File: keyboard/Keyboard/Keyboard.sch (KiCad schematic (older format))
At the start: 44 parts, among them J1 Conn_01x04, SW1 1, SW2 2, SW3 3, SW4 4, SW5 5, SW7 6, U1 TCA8418

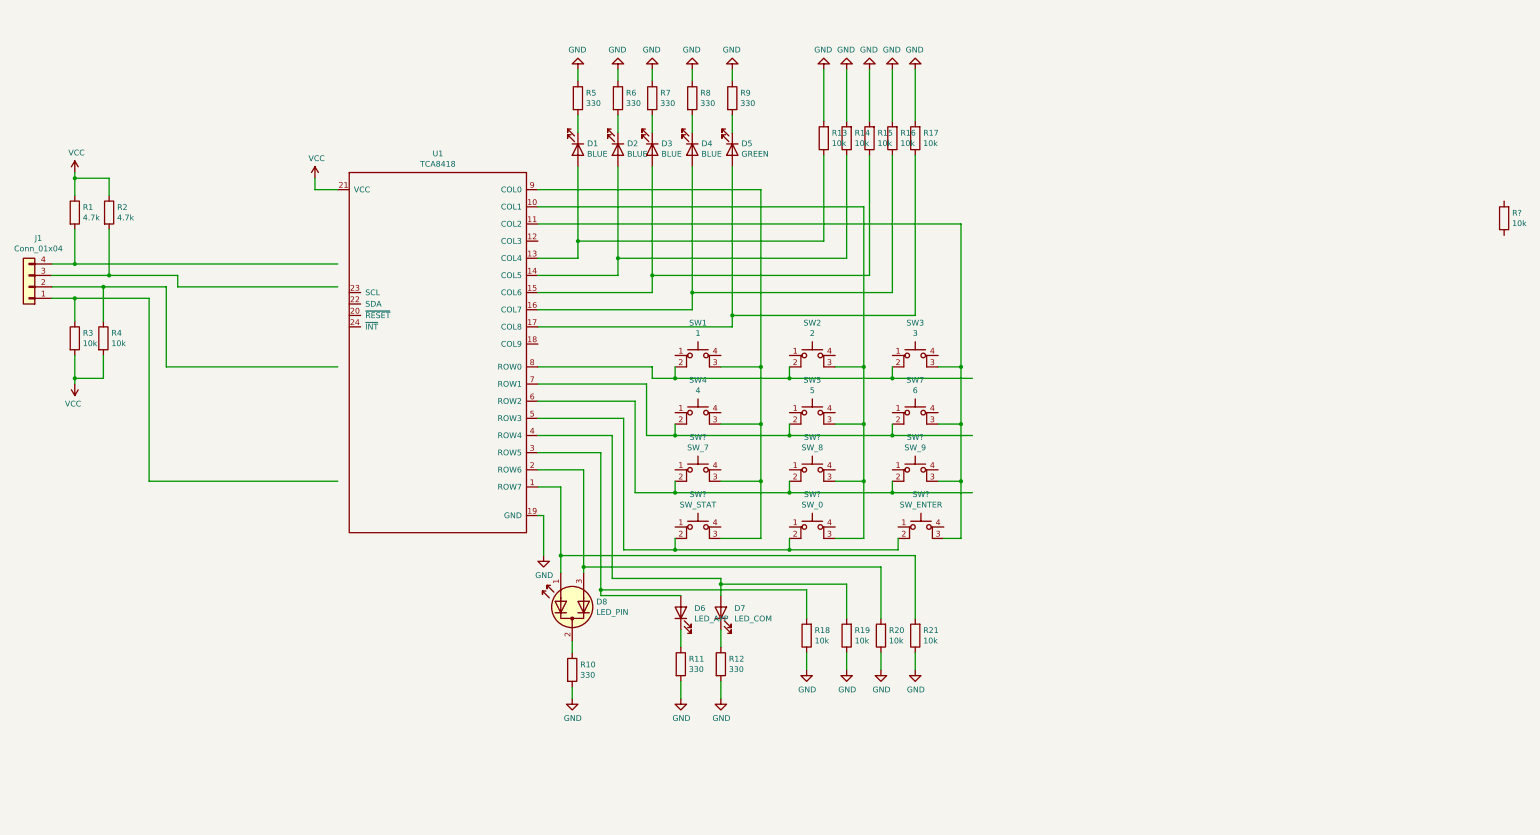
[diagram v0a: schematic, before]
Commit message: fixed pin number, added vcc, gnd header
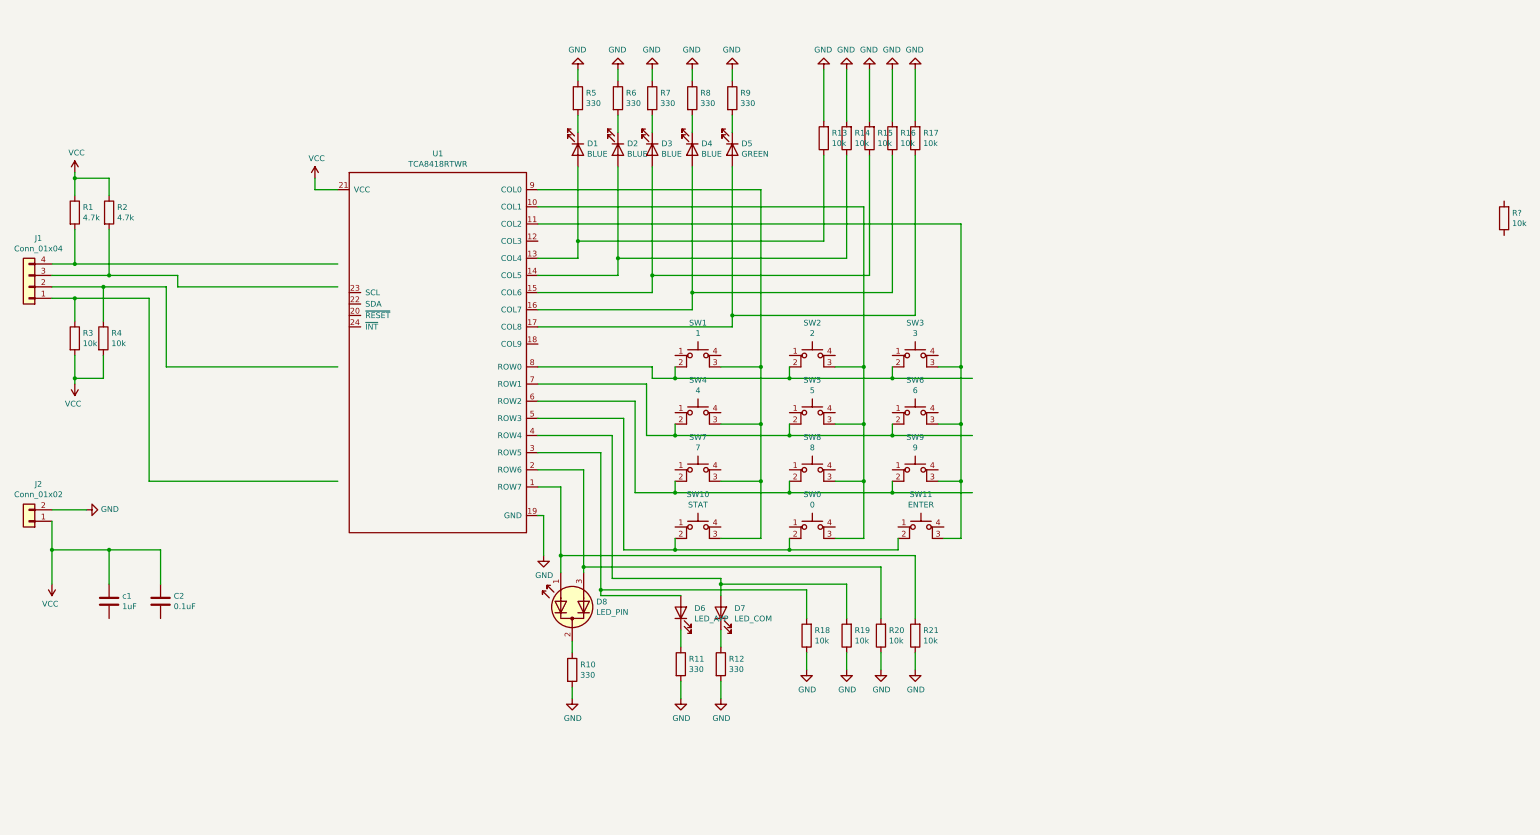
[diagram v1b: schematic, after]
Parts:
- added C2: 0.1uF, symbol Device:C
- added J2: Conn_01x02, symbol Connector_Generic:Conn_01x02
- added c1: 1uF, symbol Device:C
- SW0: renamed from SW?; value SW_0 -> 0
- SW10: renamed from SW?; value SW_STAT -> STAT
- SW11: renamed from SW?; value SW_ENTER -> ENTER
- SW7: renamed from SW?; value SW_7 -> 7
- SW8: renamed from SW?; value SW_8 -> 8
- SW9: renamed from SW?; value SW_9 -> 9
- U1: value TCA8418 -> TCA8418RTWR
- renumbered SW7 to SW6
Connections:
- wire segments 165 -> 172
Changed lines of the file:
@@
 Sheet 1 1
 Title "MixMesh keyboard"
-Date "2020-12-14"
-Rev "1.0"
+Date "2020-12-17"
+Rev "1.1"
 Comp "MixMesh"
 Comment1 ""
@@
 P 4250 3450
 F 0 "U1" H 4275 5215 50  0000 C CNN
-F 1 "TCA8418" H 4275 5124 50  0000 C CNN
+F 1 "TCA8418RTWR" H 4275 5124 50  0000 C CNN
 F 2 "" H 1300 2550 50  0001 C CNN
 F 3 "" H 1300 2550 50  0001 C CNN
@@
 $EndComp
 $Comp
-L Switch:SW_MEC_5E SW7
+L Switch:SW_MEC_5E SW6
 U 1 1 5FC76FF5
 P 8450 4050
-F 0 "SW7" H 8450 4435 50  0000 C CNN
+F 0 "SW6" H 8450 4435 50  0000 C CNN
 F 1 "6" H 8450 4344 50  0000 C CNN
 F 2 "" H 8450 4350 50  0001 C CNN
@@
 $EndComp
 $Comp
-L Switch:SW_MEC_5E SW?
+L Switch:SW_MEC_5E SW7
 U 1 1 5FC778BD
 P 6550 4550
-F 0 "SW?" H 6550 4935 50  0000 C CNN
-F 1 "SW_7" H 6550 4844 50  0000 C CNN
+F 0 "SW7" H 6550 4935 50  0000 C CNN
+F 1 "7" H 6550 4844 50  0000 C CNN
 F 2 "" H 6550 4850 50  0001 C CNN
 F 3 "http://www.apem.com/int/index.php?controller=attachment&id_attachment=1371" H 6550 4850 50  0001 C CNN
@@
 $EndComp
 $Comp
-L Switch:SW_MEC_5E SW?
+L Switch:SW_MEC_5E SW8
 U 1 1 5FC7801D
 P 7550 4550
-F 0 "SW?" H 7550 4935 50  0000 C CNN
-F 1 "SW_8" H 7550 4844 50  0000 C CNN
+F 0 "SW8" H 7550 4935 50  0000 C CNN
+F 1 "8" H 7550 4844 50  0000 C CNN
 F 2 "" H 7550 4850 50  0001 C CNN
 F 3 "http://www.apem.com/int/index.php?controller=attachment&id_attachment=1371" H 7550 4850 50  0001 C CNN
@@
 $EndComp
 $Comp
-L Switch:SW_MEC_5E SW?
+L Switch:SW_MEC_5E SW9
 U 1 1 5FC78EF4
 P 8450 4550
-F 0 "SW?" H 8450 4935 50  0000 C CNN
-F 1 "SW_9" H 8450 4844 50  0000 C CNN
+F 0 "SW9" H 8450 4935 50  0000 C CNN
+F 1 "9" H 8450 4844 50  0000 C CNN
 F 2 "" H 8450 4850 50  0001 C CNN
 F 3 "http://www.apem.com/int/index.php?controller=attachment&id_attachment=1371" H 8450 4850 50  0001 C CNN
@@
 $EndComp
 $Comp
-L Switch:SW_MEC_5E SW?
+L Switch:SW_MEC_5E SW10
 U 1 1 5FC79FBB
 P 6550 5050
-F 0 "SW?" H 6550 5435 50  0000 C CNN
-F 1 "SW_STAT" H 6550 5344 50  0000 C CNN
+F 0 "SW10" H 6550 5435 50  0000 C CNN
+F 1 "STAT" H 6550 5344 50  0000 C CNN
 F 2 "" H 6550 5350 50  0001 C CNN
 F 3 "http://www.apem.com/int/index.php?controller=attachment&id_attachment=1371" H 6550 5350 50  0001 C CNN
@@
 $EndComp
 $Comp
-L Switch:SW_MEC_5E SW?
+L Switch:SW_MEC_5E SW0
 U 1 1 5FC7A322
 P 7550 5050
-F 0 "SW?" H 7550 5435 50  0000 C CNN
-F 1 "SW_0" H 7550 5344 50  0000 C CNN
+F 0 "SW0" H 7550 5435 50  0000 C CNN
+F 1 "0" H 7550 5344 50  0000 C CNN
 F 2 "" H 7550 5350 50  0001 C CNN
 F 3 "http://www.apem.com/int/index.php?controller=attachment&id_attachment=1371" H 7550 5350 50  0001 C CNN
@@
 $EndComp
 $Comp
-L Switch:SW_MEC_5E SW?
+L Switch:SW_MEC_5E SW11
 U 1 1 5FC7A6C1
 P 8500 5050
-F 0 "SW?" H 8500 5435 50  0000 C CNN
-F 1 "SW_ENTER" H 8500 5344 50  0000 C CNN
+F 0 "SW11" H 8500 5435 50  0000 C CNN
+F 1 "ENTER" H 8500 5344 50  0000 C CNN
 F 2 "" H 8500 5350 50  0001 C CNN
 F 3 "http://www.apem.com/int/index.php?controller=attachment&id_attachment=1371" H 8500 5350 50  0001 C CNN
@@
 	5150 2150 8000 2150
 Wire Wire Line
-	8000 2150 8000 3550
-Wire Wire Line
 	5150 2300 8850 2300
-Wire Wire Line
-	8850 2300 8850 3550
 Wire Wire Line
 	8650 3550 8850 3550
@@
 Wire Wire Line
 	7750 3550 8000 3550
-Connection ~ 8000 3550
 Wire Wire Line
 	8000 3550 8000 4050
@@
 	5850 2750 5150 2750
 Wire Wire Line
-	6150 1800 6150 2750
-Wire Wire Line
 	6150 2900 5150 2900
 Wire Wire Line
@@
 Wire Wire Line
 	8850 5050 8700 5050
-Connection ~ 8850 3550
 Wire Wire Line
 	8650 4050 8850 4050
@@
 	5500 2450 5500 2600
 Wire Wire Line
-	5850 1800 5850 2600
-Connection ~ 5850 2600
-Wire Wire Line
-	5850 2600 5850 2750
-Wire Wire Line
-	8050 1700 8050 2750
-Wire Wire Line
-	8050 2750 6150 2750
-Connection ~ 6150 2750
-Wire Wire Line
-	6150 2750 6150 2900
-Wire Wire Line
-	8450 1700 8450 3100
-Wire Wire Line
 	8450 3100 6850 3100
 Connection ~ 6850 3100
@@
 	6850 3100 6850 3200
 Wire Wire Line
-	8250 1700 8250 2900
-Wire Wire Line
 	8250 2900 6500 2900
 Connection ~ 6500 2900
 Wire Wire Line
 	6500 2900 6500 3050
-Wire Wire Line
-	7850 1700 7850 2600
-Wire Wire Line
-	5850 2600 7850 2600
 Wire Wire Line
 	7650 1700 7650 2450
@@
 Wire Wire Line
 	5350 5200 5350 5350
+$Comp
+L Device:C c1
+U 1 1 5FDC4FA0
+P 1400 5600
+F 0 "c1" H 1515 5646 50  0000 L CNN
+F 1 "1uF" H 1515 5555 50  0000 L CNN
+F 2 "" H 1438 5450 50  0001 C CNN
+F 3 "~" H 1400 5600 50  0001 C CNN
+	1    1400 5600
+	1    0    0    -1
+$EndComp
+$Comp
+L Device:C C2
+U 1 1 5FDC5C48
+P 1850 5600
+F 0 "C2" H 1965 5646 50  0000 L CNN
+F 1 "0.1uF" H 1965 5555 50  0000 L CNN
+F 2 "" H 1888 5450 50  0001 C CNN
+F 3 "~" H 1850 5600 50  0001 C CNN
+	1    1850 5600
+	1    0    0    -1
+$EndComp
+$Comp
+L Connector_Generic:Conn_01x02 J2
+U 1 1 5FDDA441
+P 700 4900
+F 0 "J2" H 618 4575 50  0000 C CNN
+F 1 "Conn_01x02" H 618 4666 50  0000 C CNN
+F 2 "" H 700 4900 50  0001 C CNN
+F 3 "~" H 700 4900 50  0001 C CNN
+	1    700  4900
+	-1   0    0    1
+$EndComp
+$Comp
+L power:VCC #PWR?
+U 1 1 5FDDCD5B
+P 900 5450
+F 0 "#PWR?" H 900 5300 50  0001 C CNN
+F 1 "VCC" H 915 5623 50  0000 C CNN
+F 2 "" H 900 5450 50  0001 C CNN
+F 3 "" H 900 5450 50  0001 C CNN
+	1    900  5450
+	-1   0    0    1
+$EndComp
+Connection ~ 6150 2750
+Connection ~ 5850 2600
+Wire Wire Line
+	5850 2600 5850 2750
+Wire Wire Line
+	5850 1800 5850 2600
+Connection ~ 8850 3550
+Wire Wire Line
+	6150 2750 6150 2900
+Wire Wire Line
+	6150 1800 6150 2750
+Connection ~ 8000 3550
+Wire Wire Line
+	5850 2600 7850 2600
+Wire Wire Line
+	7850 1700 7850 2600
+Wire Wire Line
+	8250 1700 8250 2900
+Wire Wire Line
+	8450 1700 8450 3100
+Wire Wire Line
+	8050 2750 6150 2750
+Wire Wire Line
+	8050 1700 8050 2750
+Wire Wire Line
+	8850 2300 8850 3550
+Wire Wire Line
+	8000 2150 8000 3550
+$Comp
+L power:GND #PWR?
+U 1 1 5FE49D2B
+P 1200 4800
+F 0 "#PWR?" H 1200 4550 50  0001 C CNN
+F 1 "GND" V 1205 4672 50  0000 R CNN
+F 2 "" H 1200 4800 50  0001 C CNN
+F 3 "" H 1200 4800 50  0001 C CNN
+	1    1200 4800
+	0    -1   -1   0
+$EndComp
+Wire Wire Line
+	900  4900 900  5150
+Wire Wire Line
+	900  5150 1400 5150
+Wire Wire Line
+	1850 5150 1850 5450
+Connection ~ 900  5150
+Wire Wire Line
+	900  5150 900  5450
+Wire Wire Line
+	1400 5150 1400 5450
+Connection ~ 1400 5150
+Wire Wire Line
+	1400 5150 1850 5150
+Wire Wire Line
+	900  4800 1200 4800
 $EndSCHEMATC

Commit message: added PWM to be able to dim all LEDS with one control, each LED is still controlled with an output, added COL9 as GPIO, may be needed
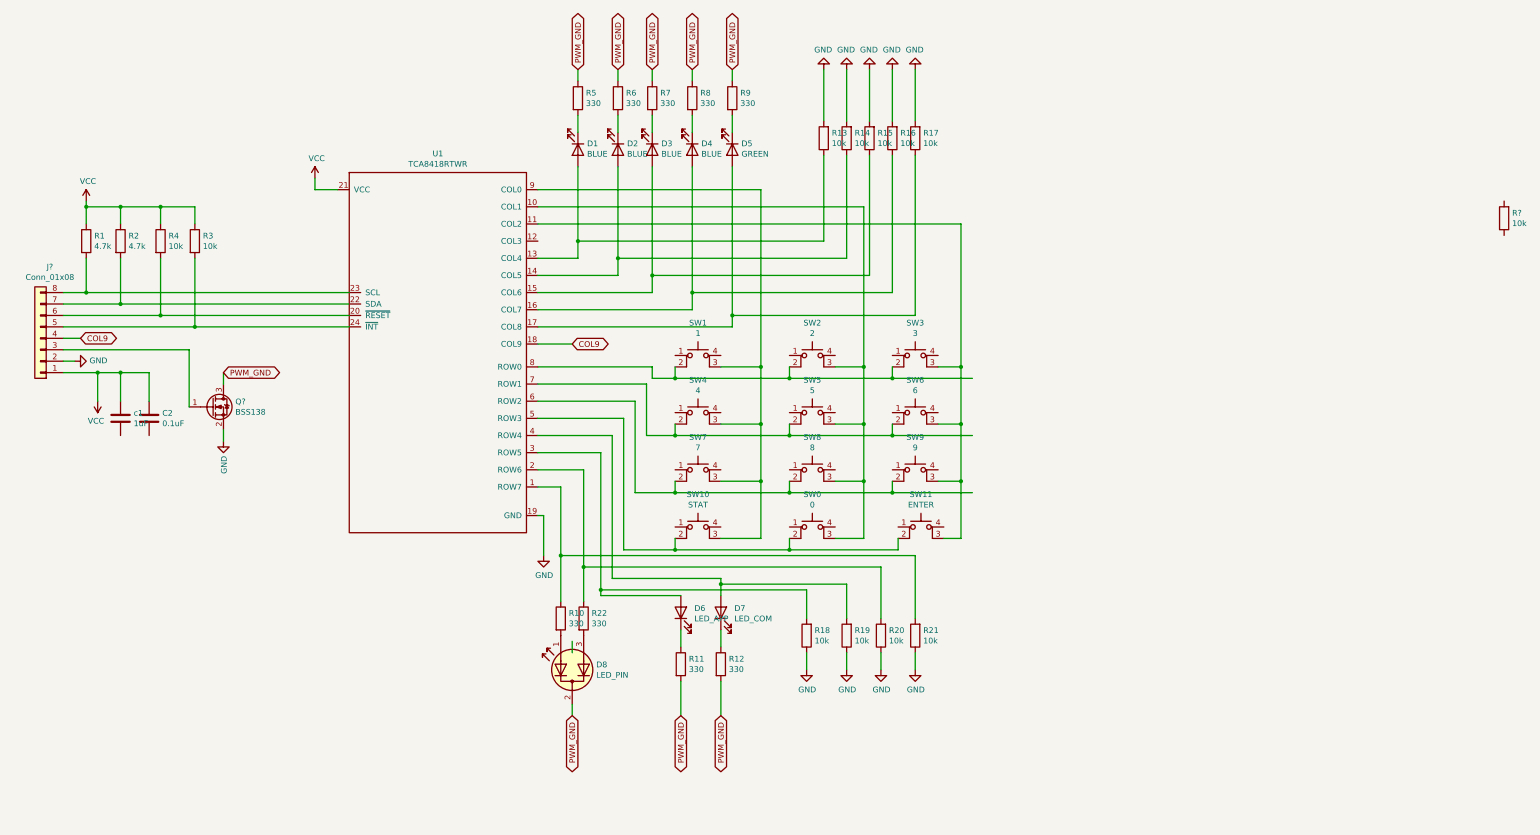
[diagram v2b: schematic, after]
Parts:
- removed J1: Conn_01x04, symbol Connector_Generic:Conn_01x04
- removed J2: Conn_01x02, symbol Connector_Generic:Conn_01x02
- added J?: Conn_01x08, symbol Connector_Generic:Conn_01x08
- added Q?: BSS138, Package_TO_SOT_SMD:SOT-23, symbol Transistor_FET:BSS138
- added R22: 330, symbol Device:R
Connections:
- net labels added: COL9, PWM_GND
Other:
- moved on the sheet: C2, D8, R1, R10, R2, R3, R4, c1

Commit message: move COL8-4 to COL7-3, using COL8,COL9 as GPIO, added R4.7k as resistor on MOS gate
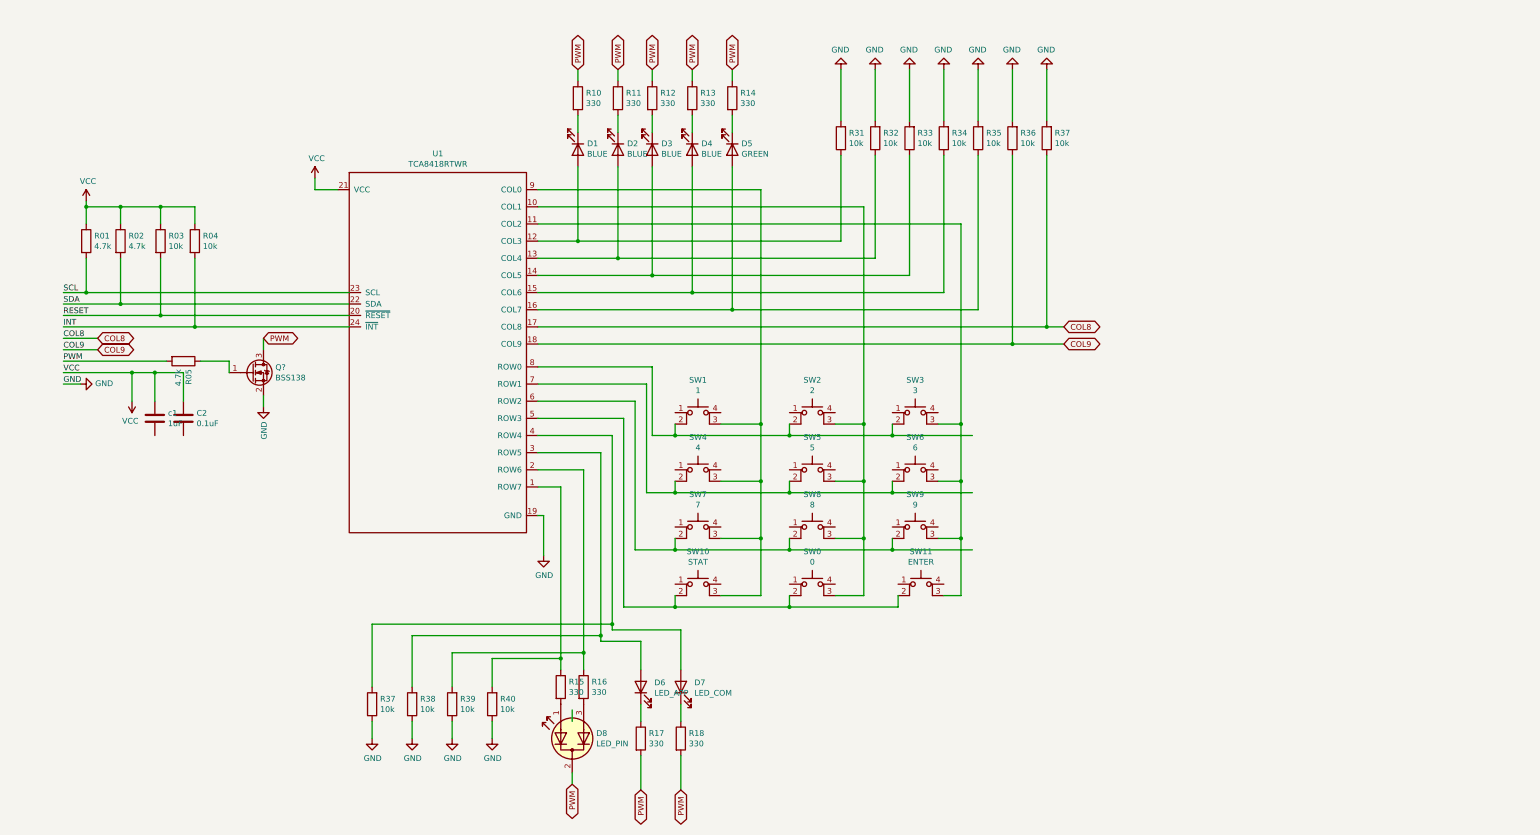
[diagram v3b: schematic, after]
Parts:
- removed J?: Conn_01x08, symbol Connector_Generic:Conn_01x08
- removed R?: 10k, symbol Device:R
- added R05: 4.7k, symbol Device:R
- added R36, R37: 10k, symbol Device:R
- renumbered R1 to R01, R2 to R02, R4 to R03, R3 to R04, R5 to R10, R6 to R11, R7 to R12, R8 to R13, R9 to R14, R10 to R15, R22 to R16, R11 to R17, R12 to R18, R13 to R31, R14 to R32, R15 to R33, R16 to R34, R17 to R35, R21 to R37, R20 to R38, R19 to R39, R18 to R40
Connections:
- net labels added: COL8, INT, PWM, RESET, SCL, SDA
- net labels removed: PWM_GND
- wire segments 172 -> 177
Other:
- moved on the sheet: C2, D6, D7, D8, Q?, R15, R16, R17, R18, R31, R32, R33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

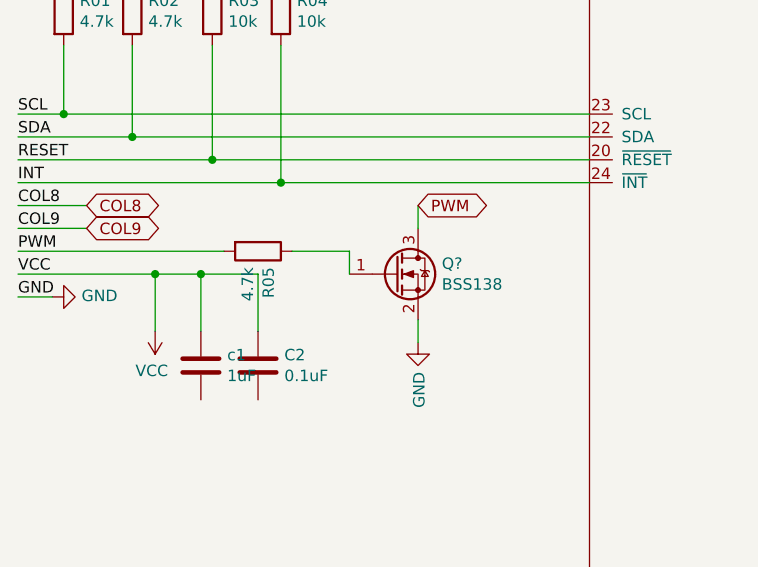
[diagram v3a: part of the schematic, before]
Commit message: scaled epxmesh demo, moved led names to match real keybaord
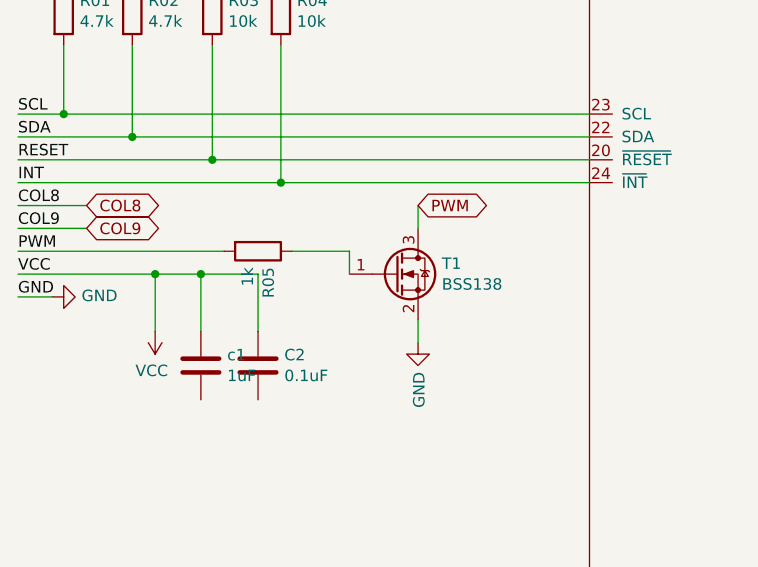
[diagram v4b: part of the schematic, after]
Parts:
- R05: value 4.7k -> 1k
- gave numbers to parts that had none: 1
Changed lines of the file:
@@
 Connection ~ 1800 3600
 $Comp
-L Transistor_FET:BSS138 Q?
+L Transistor_FET:BSS138 T1
 U 1 1 6019A453
 P 2650 3600
-F 0 "Q?" H 2854 3646 50  0000 L CNN
+F 0 "T1" H 2854 3646 50  0000 L CNN
 F 1 "BSS138" H 2854 3555 50  0000 L CNN
 F 2 "Package_TO_SOT_SMD:SOT-23" H 2850 3525 50  0001 L CIN
@@
 P 2050 3500
 F 0 "R05" H 2120 3546 50  0000 L CNN
-F 1 "4.7k" H 2120 3455 50  0000 L CNN
+F 1 "1k" H 2120 3455 50  0000 L CNN
 F 2 "" V 1980 3500 50  0001 C CNN
 F 3 "~" H 2050 3500 50  0001 C CNN

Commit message: updated schema
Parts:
- renumbered R37 to R41
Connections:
- net labels added: 1-VCC, 10-GND, 2-INT, 4-SCL, 5-PWM, 6-SDA, 7-COL8, 8-RESET, 9-COL9
- net labels removed: INT, RESET, SCL, SDA
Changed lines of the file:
@@
 Sheet 1 1
 Title "MixMesh keyboard"
-Date "2021-01-01"
-Rev "1.2"
+Date "2021-03-12"
+Rev "1.3"
 Comp "MixMesh"
 Comment1 ""
@@
 Connection ~ 6850 3050
 $Comp
-L Device:R R37
+L Device:R R41
 U 1 1 6055B086
 P 9600 1550
-F 0 "R37" H 9530 1504 50  0000 R CNN
+F 0 "R41" H 9530 1504 50  0000 R CNN
 F 1 "10k" H 9530 1595 50  0000 R CNN
 F 2 "" V 9530 1550 50  0001 C CNN
@@
 	1150 3700 1000 3700
 Text Label 1000 2900 0    50   ~ 0
-SCL
+4-SCL
 Text Label 1000 3000 0    50   ~ 0
-SDA
+6-SDA
 Text Label 1000 3100 0    50   ~ 0
-RESET
+8-RESET
 Text Label 1000 3200 0    50   ~ 0
-INT
+2-INT
 Text Label 1000 3300 0    50   ~ 0
-COL8
+7-COL8
 Text Label 1000 3400 0    50   ~ 0
-COL9
+9-COL9
 Text Label 1000 3500 0    50   ~ 0
-PWM
+5-PWM
 Text Label 1000 3600 0    50   ~ 0
-VCC
+1-VCC
 Text Label 1000 3700 0    50   ~ 0
-GND
+10-GND
 Wire Wire Line
 	1000 3300 1300 3300
